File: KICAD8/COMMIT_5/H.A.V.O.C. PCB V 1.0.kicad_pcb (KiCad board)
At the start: 8 copper layers, 128 parts, among them IC2 STM32H755IIT6, J10 Conn_02x10_Top_Bottom, J2 USB_B_Micro, J3 XT60-M, J5 Conn_Coaxial, J6 Conn_Coaxial, J7 Conn_02x10_Top_Bottom, M1 SERVO1, M2 SERVO2, M3 SERVO3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

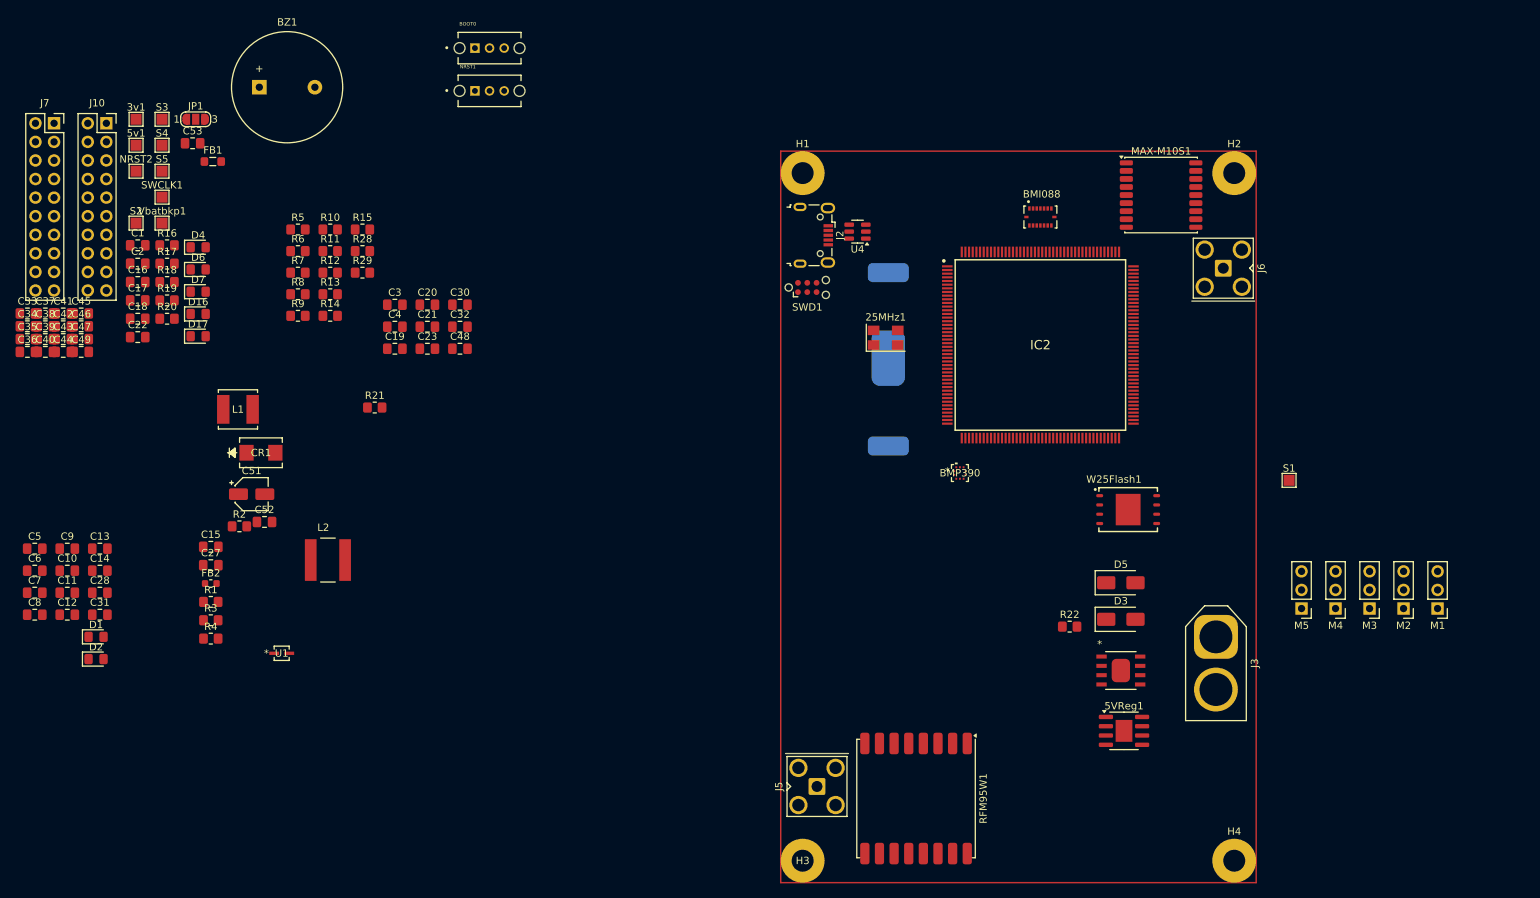
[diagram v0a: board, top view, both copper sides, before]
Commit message: Intermediary Progress on HVT2
Removed pyro circuits for cost reasons, most of layout completed, traces need to be routed still
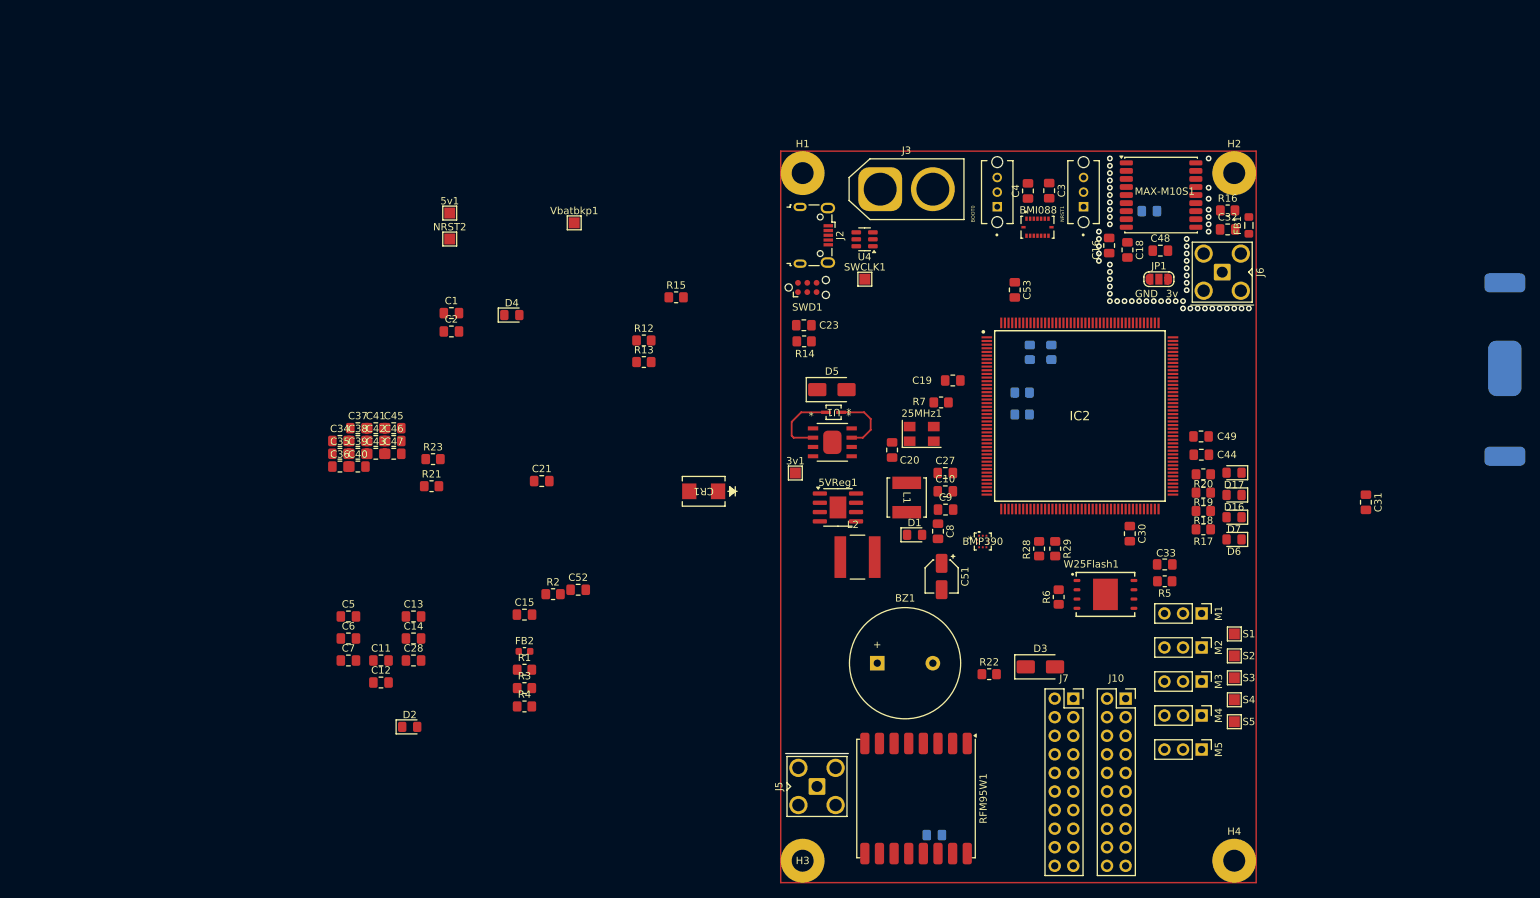
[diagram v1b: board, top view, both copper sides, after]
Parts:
- added R23: 0, Resistor_SMD:R_0805_2012Metric_Pad1.20x1.40mm_HandSolder, F.Cu at (75.0, 98.1)
- C17, C22, R10, R11, R8, R9: moved to B.Cu
- moved C31 173.8 mm to (202.5, 104.0), turned to -90 degrees
- moved S3 165.3 mm to (184.5, 128.0)
- moved S4 165.0 mm to (184.5, 131.0)
- moved S5 164.8 mm to (184.5, 134.0)
- moved S2 161.4 mm to (184.5, 125.0)
- moved J10 160.0 mm to (169.7, 130.8)
- moved J7 160.0 mm to (162.5, 130.8)
- moved C33 159.2 mm to (175.0, 112.5)
- moved C44 156.2 mm to (180.0, 97.5)
- moved C49 153.5 mm to (180.0, 95.0)
- moved D6 146.3 mm to (184.5, 109.1), turned to 180 degrees
- moved R17 146.2 mm to (180.3, 107.7), turned to 180 degrees
- moved R18 145.1 mm to (180.3, 105.2), turned to 180 degrees
- moved R16 145.1 mm to (183.6, 64.1)
- moved D7 144.9 mm to (184.5, 106.0), turned to 180 degrees
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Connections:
- net Net-(5VReg1-SW) renamed /Power/5v_sw
- 3v3Reg1 pad 1: VBAT_SWITCH -> VBAT
- C5 pad 1: VBAT_SWITCH -> VBAT
- D3 pad 1: VBAT_SWITCH -> VBAT
- D3 pad 2: 5V_OUT_USB -> Net-(D3-A)
- D5 pad 1: VBAT_SWITCH -> VBAT
- R22 pad 2: VBAT_SWITCH -> VBAT
- R28 pad 2: VBAT_SWITCH -> VBAT
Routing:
- net /Power/DRV: track 0.00 -> 10.2 mm
- net /Power/BST: track 0.00 -> 8.96 mm
- net (no net): vias 0 -> 56

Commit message: HVT2-No Traces
HVT2 layout complete, no traces yet
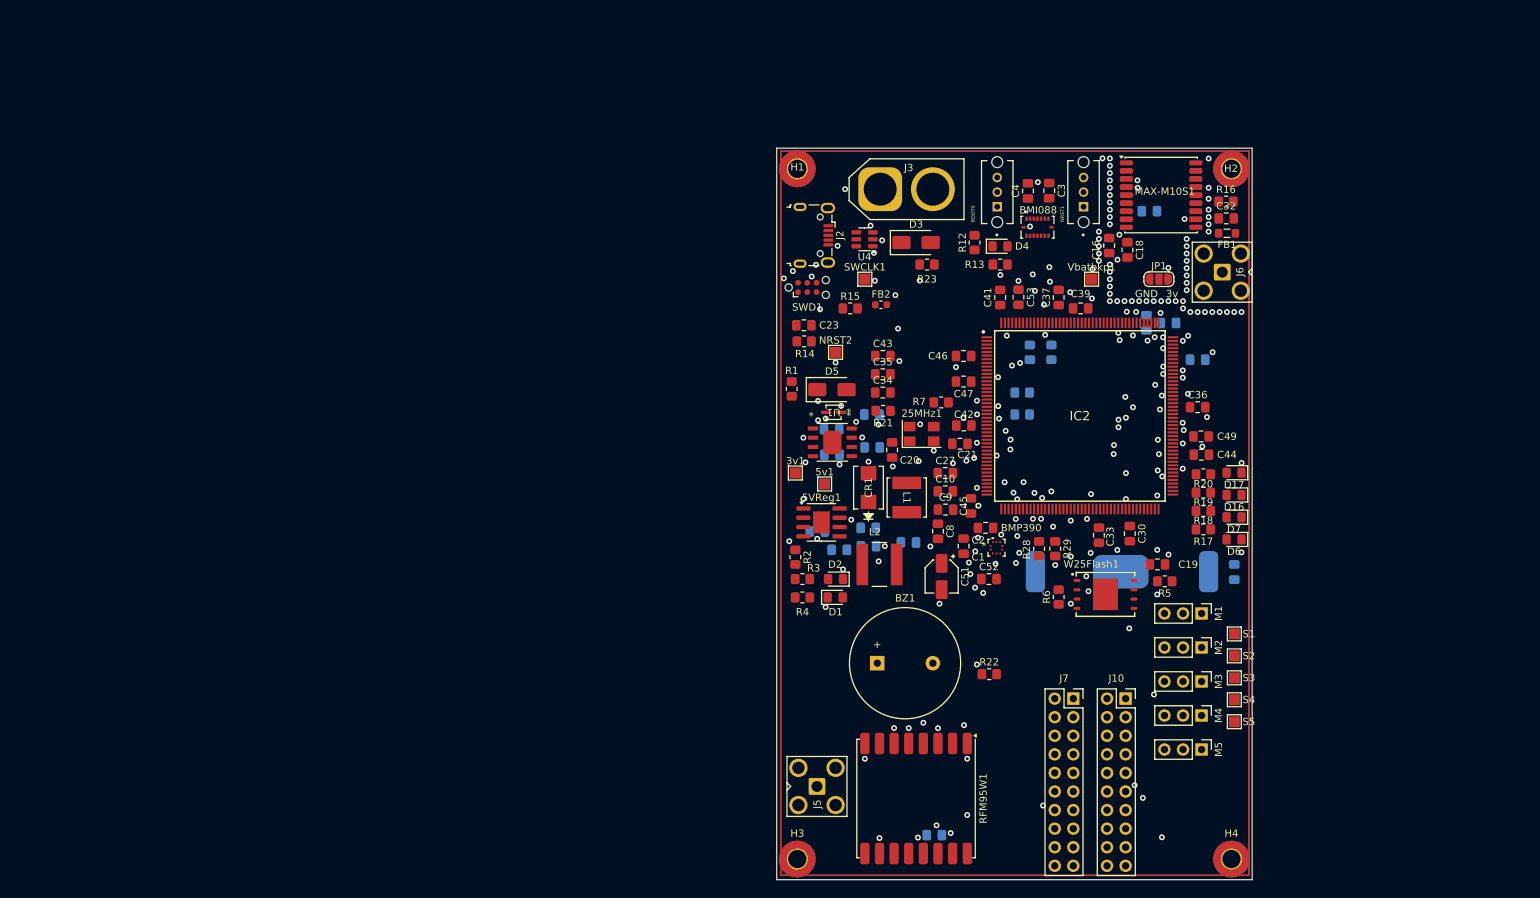
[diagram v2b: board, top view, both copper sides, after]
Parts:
- C11, C12, C13, C14, C15, C28, C31, C38, C40, C48, C5, C6, C7: moved to B.Cu
- H1, H2, H3, H4: footprint MountingHole:MountingHole_3mm_Pad -> MountingHole:MountingHole_2.5mm_Pad_TopBottom
- moved C36 117.5 mm to (179.5, 91.0)
- moved C40 115.7 mm to (179.5, 84.5)
- moved C38 109.0 mm to (172.5, 79.5), turned to -90 degrees
- moved C39 100.8 mm to (163.5, 77.5), turned to 180 degrees
- moved C37 97.5 mm to (160.5, 76.0), turned to 90 degrees
- moved C15 97.2 mm to (184.5, 113.5), turned to 90 degrees
- moved C41 87.2 mm to (152.5, 76.0), turned to 90 degrees
- moved C42 80.4 mm to (147.5, 93.5), turned to 180 degrees
- moved C45 79.6 mm to (148.5, 104.5), turned to -90 degrees
- moved C7 79.1 mm to (135.0, 92.0)
- moved C46 78.8 mm to (147.5, 84.0), turned to 180 degrees
- moved C47 78.5 mm to (147.5, 87.5), turned to 180 degrees
- moved C2 77.8 mm to (150.5, 107.5), turned to 180 degrees
- moved C1 76.9 mm to (147.5, 110.0), turned to 90 degrees
- moved C35 75.0 mm to (136.5, 86.5)
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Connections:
- net /Power/5v_sw renamed Net-(5VReg1-SW)
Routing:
- net /Power/DRV: track 10.2 -> 0.00 mm, vias 0 -> 2
- net /Power/BST: track 8.96 -> 0.00 mm, vias 0 -> 1
- net VDDA: vias 0 -> 3
- net VBat-backup: vias 0 -> 4
- net VBAT: vias 0 -> 2
- net USB_D-: vias 0 -> 3
- net USB_D+: vias 0 -> 2
- net UART5_TX: vias 0 -> 2
- net UART5_RX: vias 0 -> 2
- net UART4_TX: vias 0 -> 1
- net UART4_RX: vias 0 -> 1
- net SWO: vias 0 -> 2
- net SWDIO: vias 0 -> 1
- net SWCLK: vias 0 -> 3
- net SPI5_SCK: vias 0 -> 1
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- added copper zone on In1.Cu, net GND
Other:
- board outline added: 65 x 100 mm

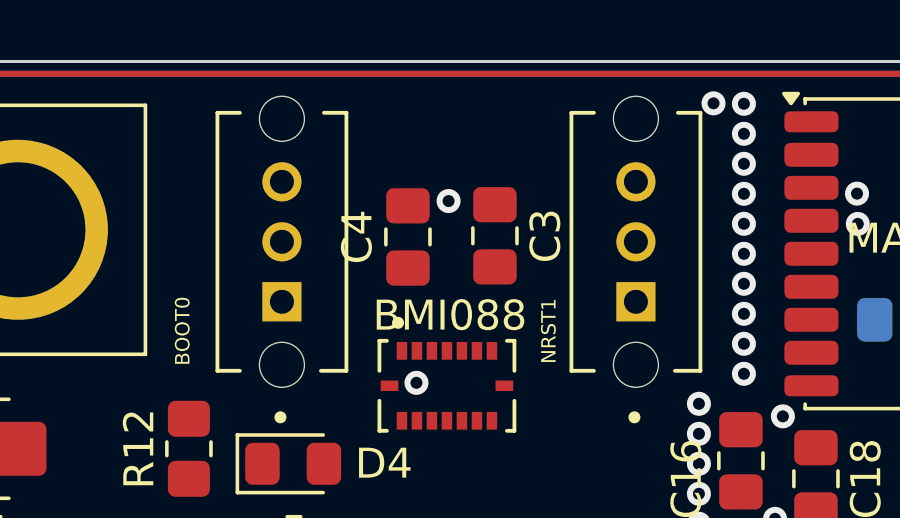
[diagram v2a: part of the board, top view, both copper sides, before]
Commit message: Changes to gnd planes
Modified gnd planes- bckp before routing/scripting
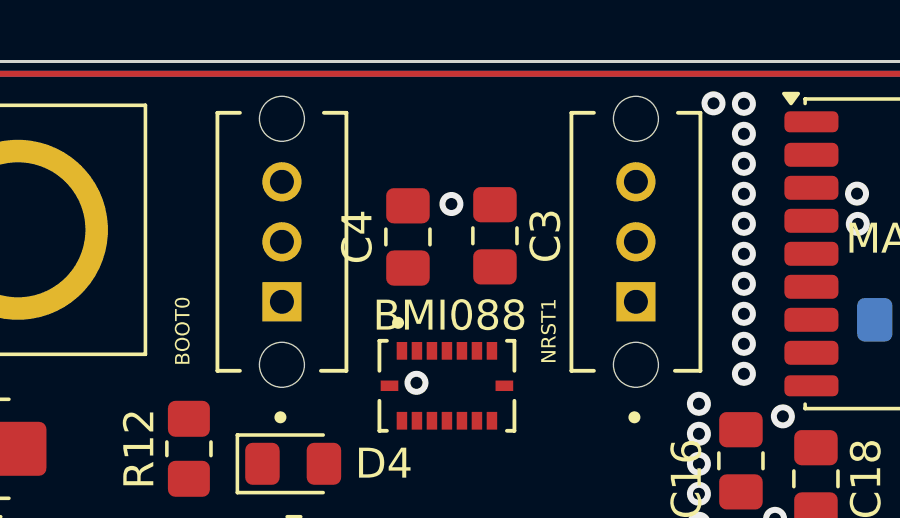
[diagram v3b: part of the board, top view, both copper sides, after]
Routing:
- added copper zone on In2.Cu, net +3V3
- added copper zone on In4.Cu, net GND
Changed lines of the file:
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@@
 			(remove_unused_layers yes)
 			(keep_end_layers yes)
-			(zone_layer_connections "In1.Cu")
+			(zone_layer_connections "In1.Cu" "In4.Cu")
 			(net 2 "GND")
 			(pinfunction "Ext")
@@
 			(remove_unused_layers yes)
 			(keep_end_layers yes)
-			(zone_layer_connections "In1.Cu")
+			(zone_layer_connections "In1.Cu" "In4.Cu")
 			(net 2 "GND")
 			(pinfunction "Ext")
@@
 			(remove_unused_layers yes)
 			(keep_end_layers yes)
-			(zone_layer_connections "In1.Cu")
+			(zone_layer_connections "In1.Cu" "In4.Cu")
 			(net 2 "GND")
 			(pinfunction "Ext")
@@
 			(remove_unused_layers yes)
 			(keep_end_layers yes)
-			(zone_layer_connections "In1.Cu")
+			(zone_layer_connections "In1.Cu" "In4.Cu")
 			(net 2 "GND")
 			(pinfunction "Ext")
@@
 			(remove_unused_layers yes)
 			(keep_end_layers yes)
-			(zone_layer_connections "In1.Cu")
+			(zone_layer_connections "In1.Cu" "In4.Cu")
 			(net 2 "GND")
 			(pinfunction "Ext")
@@
 			(remove_unused_layers yes)
 			(keep_end_layers yes)
-			(zone_layer_connections "In1.Cu")
+			(zone_layer_connections "In1.Cu" "In4.Cu")
 			(net 2 "GND")
 			(pinfunction "Ext")
@@
 			(remove_unused_layers yes)
 			(keep_end_layers yes)
-			(zone_layer_connections "In1.Cu")
+			(zone_layer_connections "In1.Cu" "In4.Cu")
 			(net 2 "GND")
 			(pinfunction "Ext")
@@
 			(remove_unused_layers yes)
 			(keep_end_layers yes)
-			(zone_layer_connections "In1.Cu")
+			(zone_layer_connections "In1.Cu" "In4.Cu")
 			(net 2 "GND")
 			(pinfunction "Ext")
@@
 	)
 	(gr_rect
-		(start 122.5 56.09)
+		(start 122.5 56)
 		(end 186.5 155)
 		(stroke
@@
 	)
 	(via
-		(at 157.655 60.2417)
+		(at 157.75 60.34)
 		(size 0.8)
 		(drill 0.4)
@@
 		(min_thickness 0.25)
 		(filled_areas_thickness no)
-		(fill
+		(fill yes
 			(thermal_gap 0.5)
 			(thermal_bridge_width 0.5)
@@
 		(polygon
 			(pts
-				(xy 164.45 56.09) (xy 122.5 56) (xy 122.5 155) (xy 186.5 155) (xy 186.45 79.59) (xy 164.45 79.34)
+				(xy 164.45 56.09) (xy 122.5 56) (xy 122.5 155) (xy 186.5 155) (xy 186.45 79.59) (xy 164.45 79.59)
 			)
 		)
@@
 		(min_thickness 0.25)
 		(filled_areas_thickness no)
-		(fill
+		(fill yes
+			(thermal_gap 0.5)
+			(thermal_bridge_width 0.5)
+		)
+		(polygon
+			(pts
+				(xy 186.5 56.09) (xy 186.45 78.99) (xy 177.05 78.99) (xy 177.05 77) (xy 165.5 77) (xy 165.5 56)
+			)
+		)
+	)
+	(zone
+		(net 3)
+		(net_name "+3V3")
+		(layer "In2.Cu")
+		(hatch edge 0.5)
+		(priority 2)
+		(connect_pads
+			(clearance 0)
+		)
+		(min_thickness 0.25)
+		(filled_areas_thickness no)
+		(fill yes
+			(thermal_gap 0.5)
+			(thermal_bridge_width 0.5)
+		)
+		(polygon
+			(pts
+				(xy 122.5 56) (xy 186.5 56) (xy 186.5 155) (xy 122.5 155)
+			)
+		)
+	)
+	(zone
+		(net 2)
+		(net_name "GND")
+		(layer "In4.Cu")
+		(hatch edge 0.5)
+		(priority 3)
+		(connect_pads
+			(clearance 0)
+		)
+		(min_thickness 0.25)
+		(filled_areas_thickness no)
+		(fill yes
 			(thermal_gap 0.5)
 			(thermal_bridge_width 0.5)
@@
 		(polygon
 			(pts
-				(xy 186.5 56.09) (xy 186.45 79.03) (xy 177 79) (xy 177 77) (xy 165.5 77) (xy 165.5 56)
+				(xy 122.5 56) (xy 186.5 56) (xy 186.5 155) (xy 122.5 155)
 			)
 		)

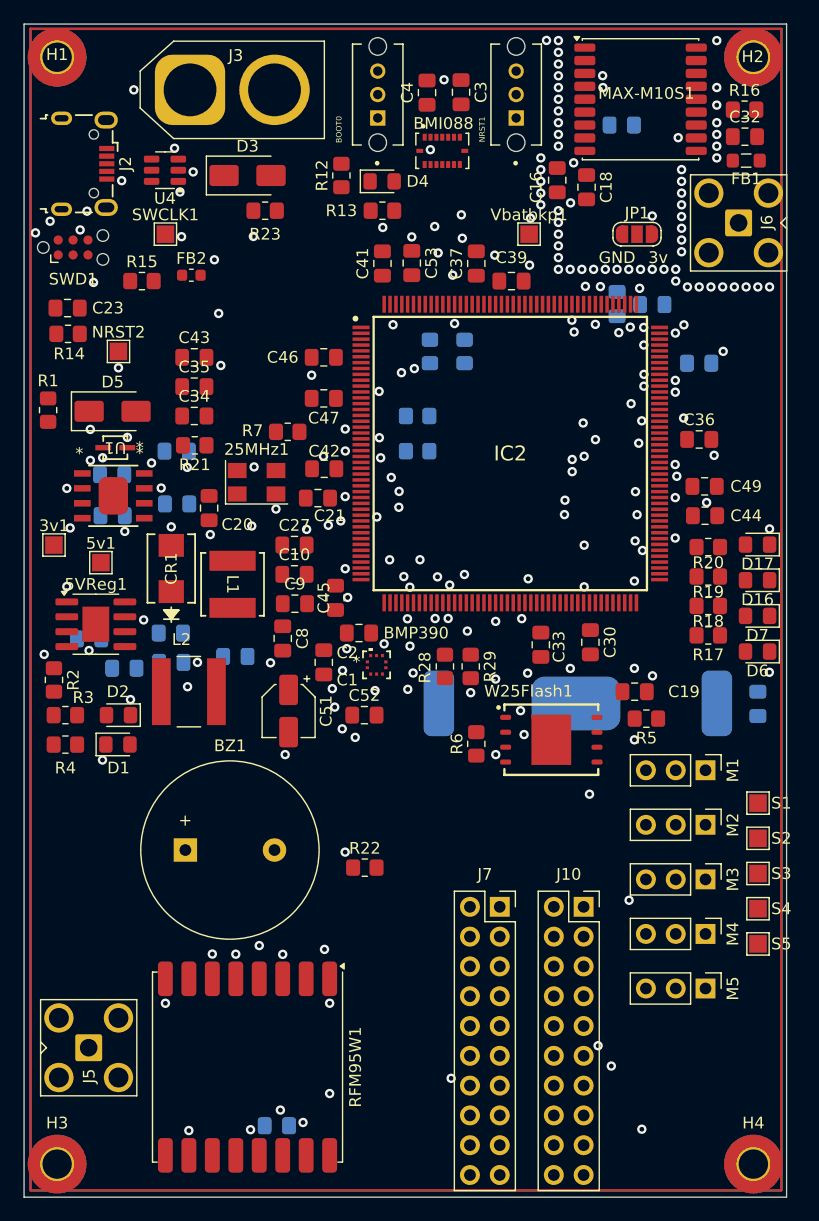
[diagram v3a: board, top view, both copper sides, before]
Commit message: Routed Traces-Preliminary
Notes:
-Differential pair is NOT routed yet
-Need to evaluate for shorts in traces/design rules
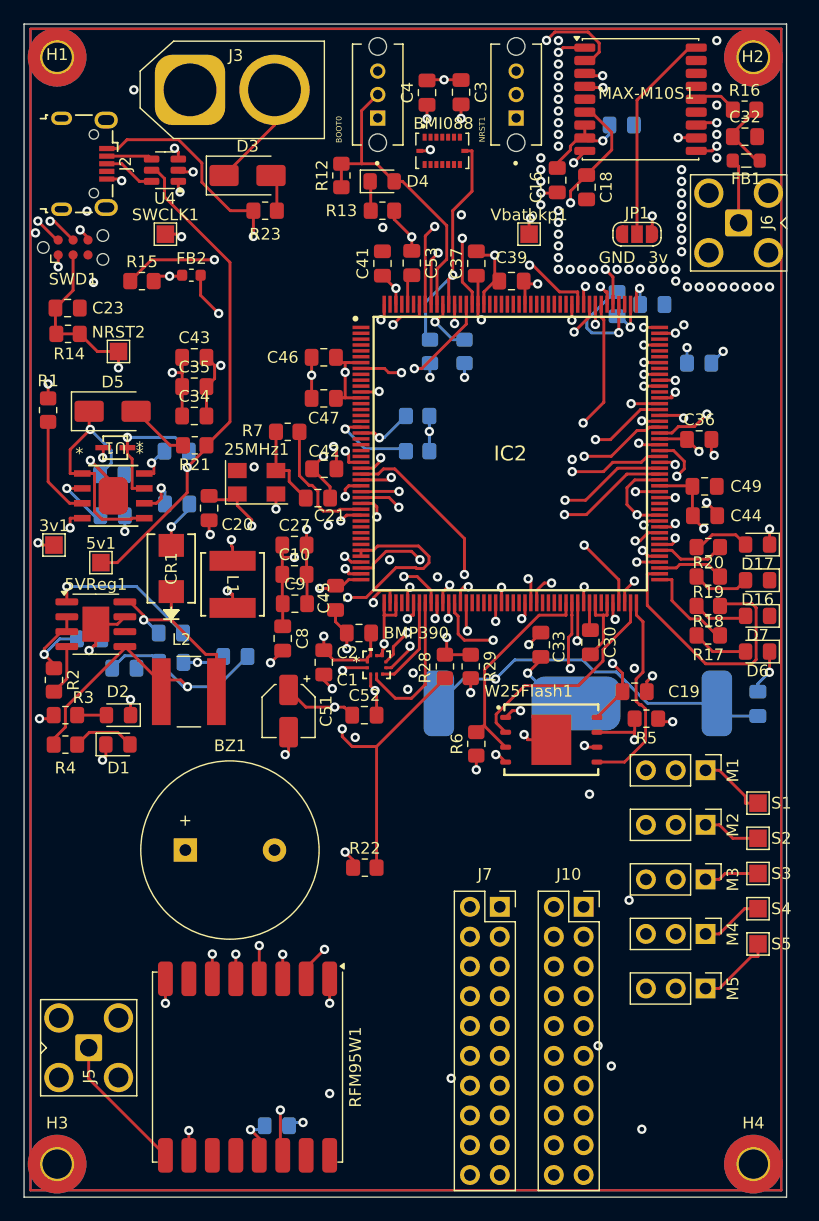
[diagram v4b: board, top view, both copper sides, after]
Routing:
- net +5V: track 0.00 -> 188.5 mm
- net GND: track 0.00 -> 159.9 mm
- net +3V3: track 0.00 -> 125.0 mm, vias 5 -> 40
- net VBAT: track 0.00 -> 122.4 mm
- net GP_GPIO34: track 0.00 -> 101.8 mm
- net VBat-backup: track 0.00 -> 98.4 mm
- net SPI3_INT: track 0.00 -> 90.9 mm
- net SPI3_MOSI: track 0.00 -> 80.0 mm
- net SPI5_CS: track 0.00 -> 79.9 mm
- net GP_GPIO35: track 0.00 -> 77.4 mm
- net NRST: track 0.00 -> 77.2 mm
- net GP_GPIO27: track 0.00 -> 73.2 mm
- net GP_GPIO29: track 0.00 -> 72.5 mm
- net SERVO5: track 0.00 -> 72.2 mm
- net GP_GPIO31: track 0.00 -> 70.9 mm
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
